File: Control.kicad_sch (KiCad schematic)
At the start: 8 parts, among them U1 XC95144XL-TQ100

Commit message: Update to new makefile, etc.
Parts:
- added J4: DBG, Connector_PinHeader_2.54mm:PinHeader_2x06_P2.54mm_Vertical, symbol Connector_Generic:Conn_02x06_Odd_Even
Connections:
- net GND: now also J4.1 (Pin_1), J4.11 (Pin_11), J4.3 (Pin_3), J4.5 (Pin_5), J4.7 (Pin_7), J4.9 (Pin_9)
- net DBG5: now reaches U1.1 (I/O/GTS3)
- net DBG5: now also J4.12 (Pin_12)
- net DBG3: now reaches U1.39 (P39)
- net DBG3: now also J4.8 (Pin_8)
- net DBG2: now reaches U1.49 (P49)
- net DBG2: now also J4.6 (Pin_6)
- net DBG1: now reaches U1.68 (P68)
- net DBG1: now also J4.4 (Pin_4)
- net DBG4: now reaches U1.71 (P71)
- net DBG4: now also J4.10 (Pin_10)
- net SW2 renamed DBG0
- net DBG0: now also J4.2 (Pin_2)
- no-connect marks 6 -> 1
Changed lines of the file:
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@@
   (junction (at 182.88 157.48) (diameter 0) (color 0 0 0 0)
   )
+  (junction (at 73.66 86.36) (diameter 0) (color 0 0 0 0)
+  )
+  (junction (at 73.66 91.44) (diameter 0) (color 0 0 0 0)
+  )
   (junction (at 119.38 186.69) (diameter 0) (color 0 0 0 0)
   )
   (junction (at 185.42 20.32) (diameter 0) (color 0 0 0 0)
   )
+  (junction (at 73.66 81.28) (diameter 0) (color 0 0 0 0)
+  )
   (junction (at 160.02 186.69) (diameter 0) (color 0 0 0 0)
   )
+  (junction (at 73.66 88.9) (diameter 0) (color 0 0 0 0)
+  )
   (junction (at 182.88 20.32) (diameter 0) (color 0 0 0 0)
   )
@@
   (junction (at 149.86 191.77) (diameter 0) (color 0 0 0 0)
   )
+  (junction (at 73.66 83.82) (diameter 0) (color 0 0 0 0)
+  )
   (junction (at 190.5 157.48) (diameter 0) (color 0 0 0 0)
   )
@@
   (junction (at 190.5 20.32) (diameter 0) (color 0 0 0 0)
   )
-  (no_connect (at 210.82 50.8))
-  (no_connect (at 210.82 35.56))
-  (no_connect (at 160.02 60.96))
   (no_connect (at 160.02 58.42))
-  (no_connect (at 210.82 127))
-  (no_connect (at 210.82 132.08))
   (bus_entry (at 147.32 63.5) (size 2.54 2.54)
     (stroke (width 0) (type default))
@@
     (stroke (width 0) (type default))
   )
+  (wire (pts (xy 73.66 81.28) (xy 73.66 83.82))
+    (stroke (width 0) (type default))
+  )
   (wire (pts (xy 160.02 33.02) (xy 149.86 33.02))
     (stroke (width 0) (type default))
@@
     (stroke (width 0) (type default))
   )
+  (wire (pts (xy 73.66 78.74) (xy 73.66 81.28))
+    (stroke (width 0) (type default))
+  )
   (bus (pts (xy 220.98 83.82) (xy 220.98 86.36))
     (stroke (width 0) (type default))
@@
     (stroke (width 0) (type default))
   )
+  (wire (pts (xy 73.66 83.82) (xy 73.66 86.36))
+    (stroke (width 0) (type default))
+  )
   (bus (pts (xy 147.32 43.18) (xy 147.32 45.72))
     (stroke (width 0) (type default))
@@
     (stroke (width 0) (type default))
   )
+  (wire (pts (xy 73.66 91.44) (xy 73.66 88.9))
+    (stroke (width 0) (type default))
+  )
   (wire (pts (xy 160.02 66.04) (xy 149.86 66.04))
+    (stroke (width 0) (type default))
+  )
+  (wire (pts (xy 73.66 86.36) (xy 73.66 88.9))
     (stroke (width 0) (type default))
   )
@@
     (effects (font (size 1.27 1.27)) (justify left bottom))
   )
+  (label "DBG3" (at 210.82 35.56 0) (fields_autoplaced)
+    (effects (font (size 1.27 1.27)) (justify left bottom))
+  )
+  (label "DBG5" (at 86.36 91.44 0) (fields_autoplaced)
+    (effects (font (size 1.27 1.27)) (justify left bottom))
+  )
   (label "RA11" (at 210.82 114.3 0) (fields_autoplaced)
     (effects (font (size 1.27 1.27)) (justify left bottom))
@@
     (effects (font (size 1.27 1.27)) (justify right bottom))
   )
+  (label "DBG1" (at 86.36 81.28 0) (fields_autoplaced)
+    (effects (font (size 1.27 1.27)) (justify left bottom))
+  )
   (label "A5" (at 160.02 63.5 180) (fields_autoplaced)
     (effects (font (size 1.27 1.27)) (justify right bottom))
   )
-  (label "SW2" (at 210.82 124.46 0) (fields_autoplaced)
-    (effects (font (size 1.27 1.27)) (justify left bottom))
-  )
   (label "RA2" (at 210.82 45.72 0) (fields_autoplaced)
     (effects (font (size 1.27 1.27)) (justify left bottom))
@@
     (effects (font (size 1.27 1.27)) (justify left bottom))
   )
+  (label "DBG5" (at 160.02 60.96 180) (fields_autoplaced)
+    (effects (font (size 1.27 1.27)) (justify right bottom))
+  )
   (label "A16" (at 160.02 35.56 180) (fields_autoplaced)
     (effects (font (size 1.27 1.27)) (justify right bottom))
@@
     (effects (font (size 1.27 1.27)) (justify right bottom))
   )
+  (label "DBG1" (at 210.82 127 0) (fields_autoplaced)
+    (effects (font (size 1.27 1.27)) (justify left bottom))
+  )
   (label "A9" (at 160.02 73.66 180) (fields_autoplaced)
     (effects (font (size 1.27 1.27)) (justify right bottom))
@@
     (effects (font (size 1.27 1.27)) (justify right bottom))
   )
+  (label "DBG2" (at 210.82 50.8 0) (fields_autoplaced)
+    (effects (font (size 1.27 1.27)) (justify left bottom))
+  )
+  (label "DBG4" (at 210.82 132.08 0) (fields_autoplaced)
+    (effects (font (size 1.27 1.27)) (justify left bottom))
+  )
   (label "GA22" (at 210.82 109.22 0) (fields_autoplaced)
     (effects (font (size 1.27 1.27)) (justify left bottom))
@@
     (effects (font (size 1.27 1.27)) (justify left bottom))
   )
+  (label "DBG0" (at 210.82 124.46 0) (fields_autoplaced)
+    (effects (font (size 1.27 1.27)) (justify left bottom))
+  )
   (label "A11" (at 160.02 78.74 180) (fields_autoplaced)
     (effects (font (size 1.27 1.27)) (justify right bottom))
   )
+  (label "DBG0" (at 86.36 78.74 0) (fields_autoplaced)
+    (effects (font (size 1.27 1.27)) (justify left bottom))
+  )
   (label "A18" (at 160.02 40.64 180) (fields_autoplaced)
     (effects (font (size 1.27 1.27)) (justify right bottom))
@@
     (effects (font (size 1.27 1.27)) (justify right bottom))
   )
+  (label "DBG2" (at 86.36 83.82 0) (fields_autoplaced)
+    (effects (font (size 1.27 1.27)) (justify left bottom))
+  )
   (label "A4" (at 160.02 137.16 180) (fields_autoplaced)
     (effects (font (size 1.27 1.27)) (justify right bottom))
@@
     (effects (font (size 1.27 1.27)) (justify right bottom))
   )
+  (label "DBG4" (at 86.36 88.9 0) (fields_autoplaced)
+    (effects (font (size 1.27 1.27)) (justify left bottom))
+  )
   (label "A19" (at 160.02 43.18 180) (fields_autoplaced)
     (effects (font (size 1.27 1.27)) (justify right bottom))
@@
   )
   (label "GA23" (at 223.52 106.68 0) (fields_autoplaced)
+    (effects (font (size 1.27 1.27)) (justify left bottom))
+  )
+  (label "DBG3" (at 86.36 86.36 0) (fields_autoplaced)
     (effects (font (size 1.27 1.27)) (justify left bottom))
   )
@@
         )
       )
+    )
+  )
+  (symbol (lib_id "power:GND") (at 73.66 91.44 0) (unit 1)
+    (in_bom yes) (on_board yes) (dnp no)
+    (property "Reference" "#PWR024" (at 73.66 97.79 0)
+      (effects (font (size 1.27 1.27)) hide)
+    )
+    (property "Value" "GND" (at 73.66 95.25 0)
+      (effects (font (size 1.27 1.27)))
+    )
+    (property "Footprint" "" (at 73.66 91.44 0)
+      (effects (font (size 1.27 1.27)) hide)
+    )
+    (property "Datasheet" "" (at 73.66 91.44 0)
+      (effects (font (size 1.27 1.27)) hide)
+    )
+    (pin "1")
+    (instances
+      (project "WarpSE"
+        (path "/a5be2cb8-c68d-4180-8412-69a6b4c5b1d4/00000000-0000-0000-0000-00005f723173"
+          (reference "#PWR024") (unit 1)
+        )
+      )
+    )
+  )
+  (symbol (lib_id "Connector_Generic:Conn_02x06_Odd_Even") (at 78.74 83.82 0) (unit 1)
+    (in_bom yes) (on_board yes) (dnp no)
+    (property "Reference" "J4" (at 80.01 76.2 0)
+      (effects (font (size 1.27 1.27)))
+    )
+    (property "Value" "DBG" (at 80.01 93.98 0)
+      (effects (font (size 1.27 1.27)))
+    )
+    (property "Footprint" "Connector_PinHeader_2.54mm:PinHeader_2x06_P2.54mm_Vertical" (at 78.74 83.82 0)
+      (effects (font (size 1.27 1.27)) hide)
+    )
+    (property "Datasheet" "~" (at 78.74 83.82 0)
+      (effects (font (size 1.27 1.27)) hide)
+    )
+    (pin "1")
+    (pin "10")
+    (pin "11")
+    (pin "12")
+    (pin "2")
+    (pin "3")
+    (pin "4")
+    (pin "5")
+    (pin "6")
+    (pin "7")
+    (pin "8")
+    (pin "9")
+    (instances
+      (project "WarpSE"
+        (path "/a5be2cb8-c68d-4180-8412-69a6b4c5b1d4/00000000-0000-0000-0000-00005f723173"
+          (reference "J4") (unit 1)
+        )
+      )

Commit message: RC
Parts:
- J4: footprint Connector_PinHeader_2.54mm:PinHeader_2x06_P2.54mm_Vertical -> stdpads:PinHeader_2x06_P2.54mm_Vertical
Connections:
- net GND: no longer J4.1 (Pin_1)
- net ROM~{CS} renamed ROM~{OE}
- new net +5V: J4.1 (Pin_1)
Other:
- company: (none) -> Garrett's Workshop
- title: (none) -> WarpSE (GW4410A)
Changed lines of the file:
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@@
 (kicad_sch (version 20230121) (generator eeschema)
   (paper "A4")
+  (title_block
+    (title "WarpSE (GW4410A)")
+    (date "2024-03-27")
+    (rev "1.0")
+    (company "Garrett's Workshop")
+  )
   (junction (at 119.38 191.77) (diameter 0) (color 0 0 0 0)
   )
@@
   )
   (junction (at 185.42 20.32) (diameter 0) (color 0 0 0 0)
-  )
-  (junction (at 73.66 81.28) (diameter 0) (color 0 0 0 0)
   )
   (junction (at 160.02 186.69) (diameter 0) (color 0 0 0 0)
@@
     (stroke (width 0) (type default))
   )
-  (wire (pts (xy 73.66 78.74) (xy 73.66 81.28))
-    (stroke (width 0) (type default))
-  )
   (bus (pts (xy 220.98 83.82) (xy 220.98 86.36))
     (stroke (width 0) (type default))
@@
     (effects (font (size 1.27 1.27)) (justify left))
   )
-  (hierarchical_label "ROM~{CS}" (shape output) (at 210.82 27.94 0) (fields_autoplaced)
+  (hierarchical_label "ROM~{OE}" (shape output) (at 210.82 27.94 0) (fields_autoplaced)
     (effects (font (size 1.27 1.27)) (justify left))
   )
@@
     )
   )
+  (symbol (lib_id "power:+5V") (at 73.66 78.74 0) (unit 1)
+    (in_bom yes) (on_board yes) (dnp no)
+    (property "Reference" "#PWR07" (at 73.66 82.55 0)
+      (effects (font (size 1.27 1.27)) hide)
+    )
+    (property "Value" "+5V" (at 73.66 74.93 0)
+      (effects (font (size 1.27 1.27)))
+    )
+    (property "Footprint" "" (at 73.66 78.74 0)
+      (effects (font (size 1.27 1.27)) hide)
+    )
+    (property "Datasheet" "" (at 73.66 78.74 0)
+      (effects (font (size 1.27 1.27)) hide)
+    )
+    (pin "1")
+    (instances
+      (project "WarpSE"
+        (path "/a5be2cb8-c68d-4180-8412-69a6b4c5b1d4/00000000-0000-0000-0000-00005f723173"
+          (reference "#PWR07") (unit 1)
+        )
+      )
+    )
+  )
   (symbol (lib_id "power:GND") (at 73.66 91.44 0) (unit 1)
     (in_bom yes) (on_board yes) (dnp no)
@@
       (effects (font (size 1.27 1.27)))
     )
-    (property "Footprint" "Connector_PinHeader_2.54mm:PinHeader_2x06_P2.54mm_Vertical" (at 78.74 83.82 0)
-      (effects (font (size 1.27 1.27)) hide)
-    )
+    (property "Footprint" "stdpads:PinHeader_2x06_P2.54mm_Vertical" (at 78.74 83.82 0)
+      (effects (font (size 1.27 1.27)) hide)
+    )

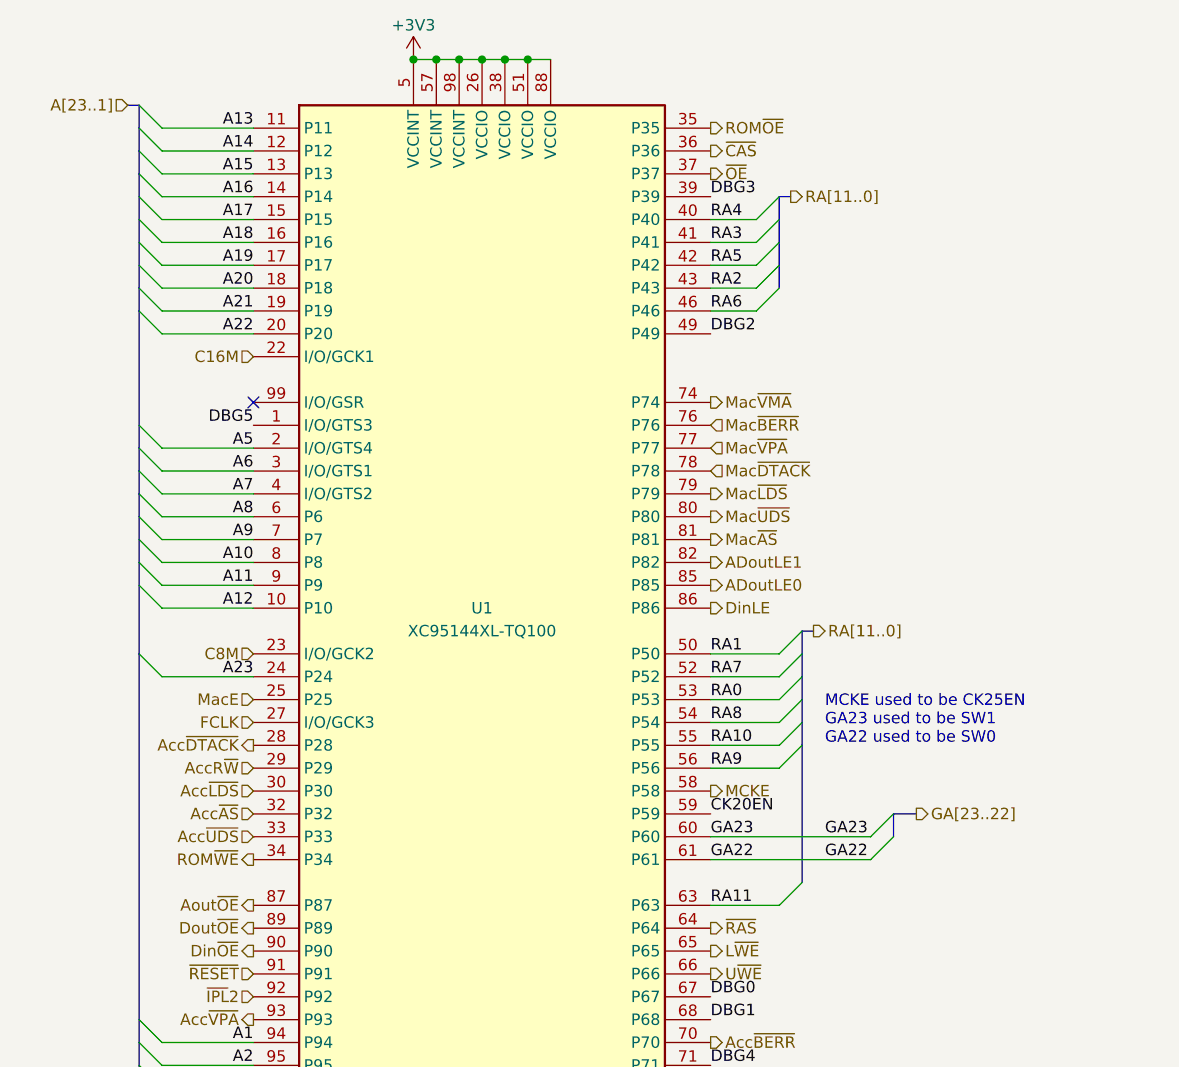
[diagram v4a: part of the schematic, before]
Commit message: Board prerelease revision 3 with USB power, A[23:20] remapping
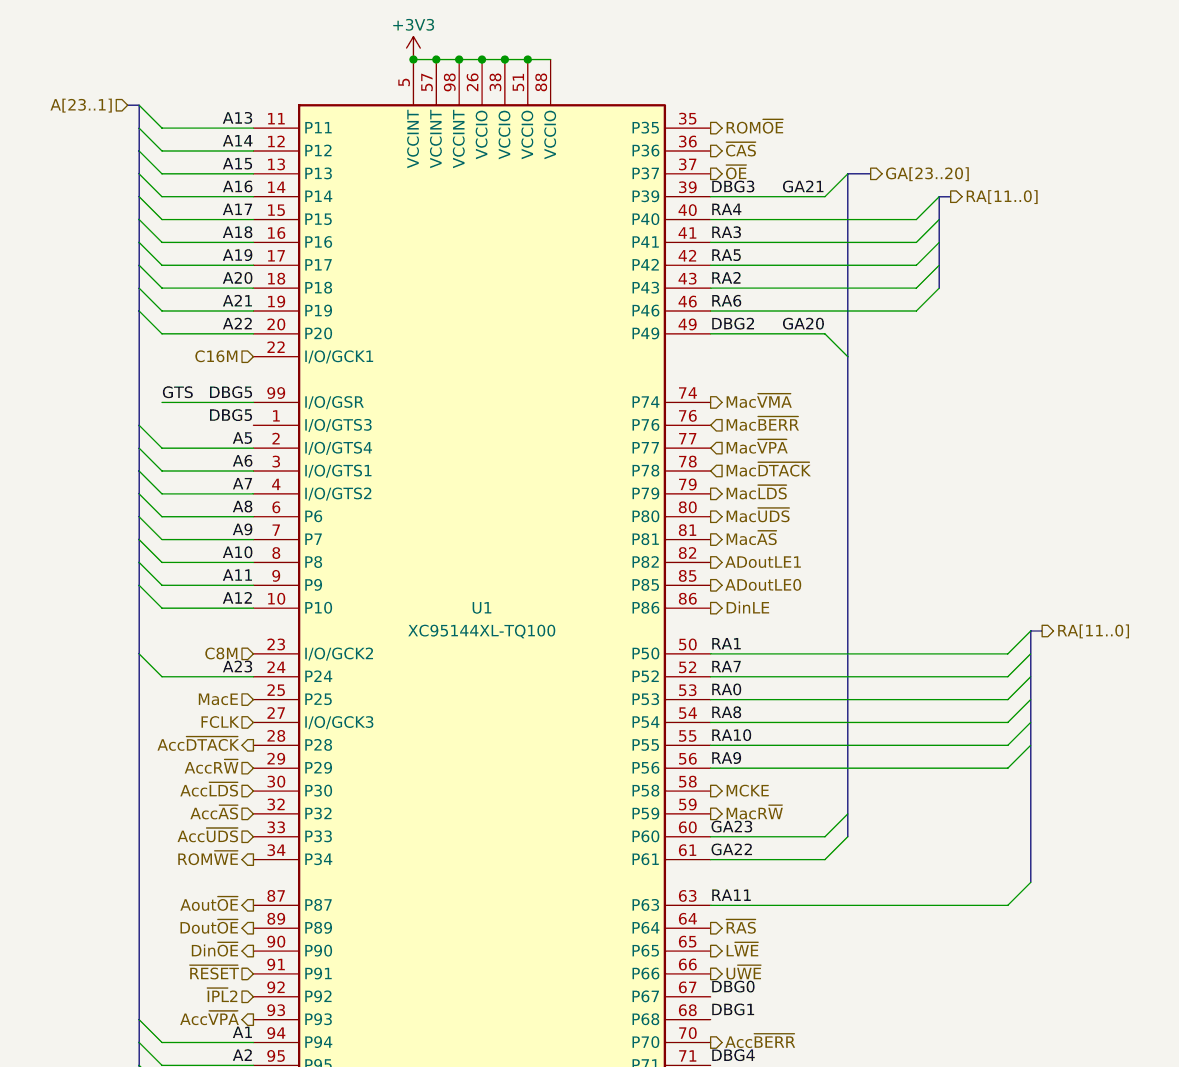
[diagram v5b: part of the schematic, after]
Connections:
- net DBG5: now also U1.99 (I/O/GSR)
- net CK20EN renamed MacR~{W}
- no-connect marks 1 -> 0
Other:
- note removed: "MCKE used to be CK25EN GA23 used to be SW1 GA22 used to be SW0"

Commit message: Before switching to SiT2001 oscillator
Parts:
- added C22, C23: 2u2, stdpads:C_0603, symbol Device:C_Small
- added R32, R33, R34, R35, R36: 1k, stdpads:R_0603, symbol Device:R_Small
- added R37: 47, stdpads:R_0603, symbol Device:R_Small
- added U29: 74LVC1G34GW, stdpads:SOT-353, symbol GW_Logic:741G32GW
- J4: footprint stdpads:PinHeader_2x06_P2.54mm_Vertical -> stdpads:PinSocket_2x06_P2.54mm_Vertical
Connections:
- net +3V3: now also C23.1, U29.5 (Vcc)
- net +5V: now also J4.2 (Pin_2), C22.1, R32.2, R33.2, R34.2, R35.2, R36.2; no longer J4.1 (Pin_1)
- net GND: now also J4.12 (Pin_12), J4.4 (Pin_4), C22.2, C23.2, U29.1 (A), U29.3 (GND); no longer J4.11 (Pin_11), J4.5 (Pin_5), J4.7 (Pin_7), J4.9 (Pin_9)
- net DBG0 renamed DBG0_ROMWS
- net DBG0_ROMWS: now also J4.6 (Pin_6), R32.1; no longer J4.2 (Pin_2)
- net DBG1 renamed DBG1_RAMWS
- net DBG1_RAMWS: now also J4.5 (Pin_5), R33.1; no longer J4.4 (Pin_4)
- net DBG2 renamed DBG2_GA20
- net DBG2_GA20: now also J4.10 (Pin_10), R36.1; no longer J4.6 (Pin_6)
- net DBG3 renamed DBG3_GA21
- net DBG3_GA21: now also J4.9 (Pin_9), R35.1; no longer J4.8 (Pin_8)
- net DBG4 renamed DBG4_IOWS
- net DBG4_IOWS: now also J4.8 (Pin_8), R34.1; no longer J4.10 (Pin_10)
- net DBG5 renamed DBG5_GTS_GOE
- net DBG5_GTS_GOE: now also J4.11 (Pin_11); no longer J4.12 (Pin_12)
- net GA23 renamed DBG6_GA23
- new net: R37.2, U29.4 (Y)
- new net CLKEN: J4.7 (Pin_7)
- new net CLKIN: R37.1
- new net CLKINu: J4.1 (Pin_1), U29.2 (B)

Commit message: Board changes
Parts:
- J4: footprint stdpads:PinSocket_2x06_P2.54mm_Vertical -> stdpads:PinSocket_2x06_P2.00mm_Vertical
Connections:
- net Mac~{BG} renamed BA18
- net RA11 renamed BA19
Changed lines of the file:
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@@
 	)
 	(bus_entry
+		(at 246.38 134.62)
+		(size -2.54 2.54)
+		(stroke
+			(width 0)
+			(type default)
+		)
+	)
+	(bus_entry
 		(at 142.24 127)
 		(size 2.54 2.54)
@@
 		)
 	)
-	(bus
-		(pts
-			(xy 246.38 96.52) (xy 246.38 111.76)
-		)
-		(stroke
-			(width 0)
-			(type default)
-		)
-	)
 	(wire
 		(pts
@@
 	(wire
 		(pts
+			(xy 210.82 137.16) (xy 243.84 137.16)
+		)
+		(stroke
+			(width 0)
+			(type default)
+		)
+	)
+	(wire
+		(pts
 			(xy 149.86 191.77) (xy 160.02 191.77)
 		)
@@
 		)
 	)
+	(bus
+		(pts
+			(xy 246.38 134.62) (xy 247.65 134.62)
+		)
+		(stroke
+			(width 0)
+			(type default)
+		)
+	)
 	(wire
 		(pts
@@
 	(bus
 		(pts
+			(xy 246.38 111.76) (xy 247.65 111.76)
+		)
+		(stroke
+			(width 0)
+			(type default)
+		)
+	)
+	(bus
+		(pts
 			(xy 246.38 35.56) (xy 247.65 35.56)
 		)
@@
 		)
 	)
-	(label "RA11"
+	(label "BA19"
 		(at 210.82 114.3 0)
 		(fields_autoplaced yes)
@@
 		)
 	)
+	(label "BA18"
+		(at 210.82 137.16 0)
+		(fields_autoplaced yes)
+		(effects
+			(font
+				(size 1.27 1.27)
+			)
+			(justify left bottom)
+		)
+	)
 	(label "GA23"
 		(at 238.76 106.68 180)
@@
 		)
 	)
-	(hierarchical_label "Mac~{BG}"
-		(shape input)
-		(at 210.82 137.16 0)
-		(fields_autoplaced yes)
-		(effects
-			(font
-				(size 1.27 1.27)
-			)
-			(justify left)
-		)
-	)
 	(hierarchical_label "Acc~{UDS}"
 		(shape input)
@@
 		)
 	)
+	(hierarchical_label "BA[19..18]"
+		(shape output)
+		(at 247.65 134.62 0)
+		(fields_autoplaced yes)
+		(effects
+			(font
+				(size 1.27 1.27)
+			)
+			(justify left)
+		)
+	)
 	(hierarchical_label "~{IPL}2"
 		(shape input)
@@
 		)
 	)
+	(hierarchical_label "BA[19..18]"
+		(shape output)
+		(at 247.65 111.76 0)
+		(fields_autoplaced yes)
+		(effects
+			(font
+				(size 1.27 1.27)
+			)
+			(justify left)
+		)
+	)
 	(hierarchical_label "Mac~{BERR}"
 		(shape input)
@@
 			)
 		)
-		(property "Footprint" "stdpads:PinSocket_2x06_P2.54mm_Vertical"
+		(property "Footprint" "stdpads:PinSocket_2x06_P2.00mm_Vertical"
 			(at 76.2 88.9 0)
 			(effects
